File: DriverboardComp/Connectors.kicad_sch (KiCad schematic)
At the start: 14 parts, among them J26 IR Controller, J4 Kicker, J5 NUCLEO, Q6 PMOS

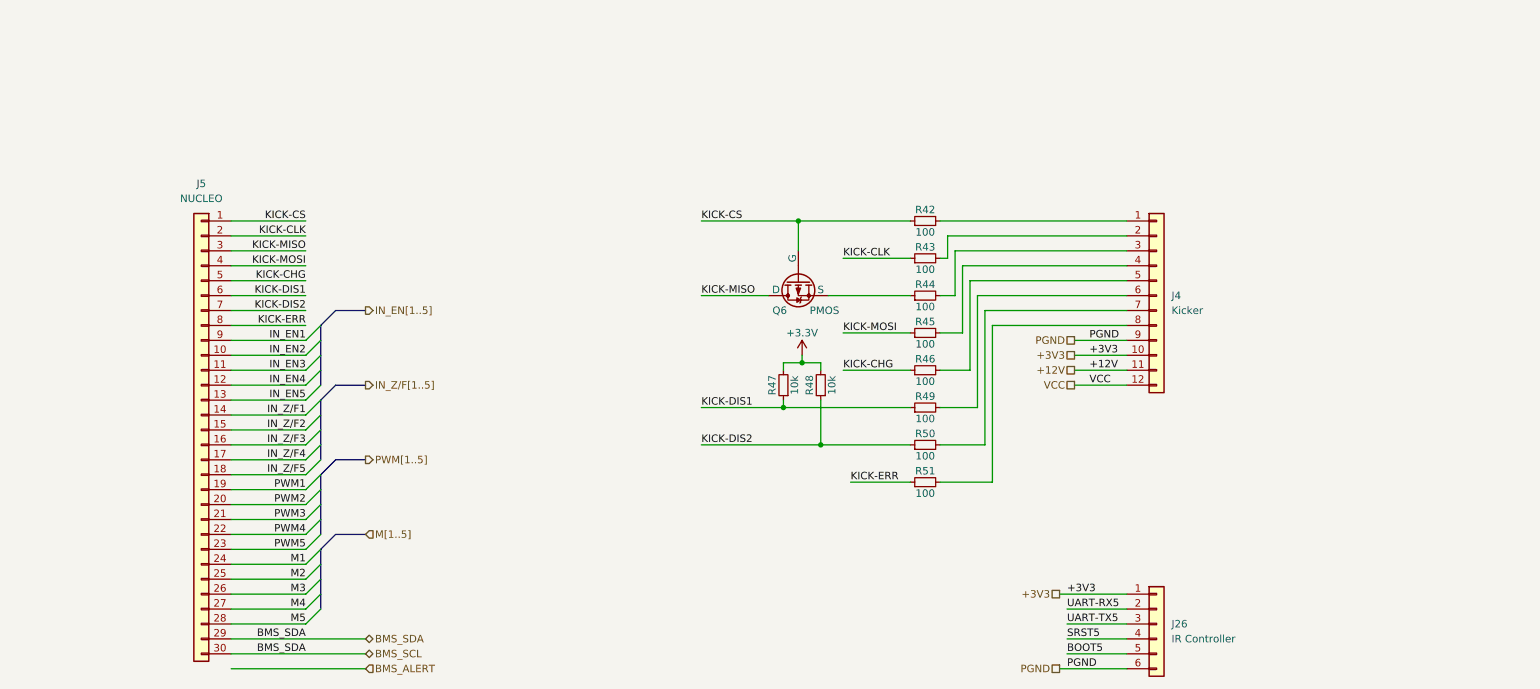
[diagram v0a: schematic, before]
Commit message: DriverboardComp is the complete design, need to be evaluated
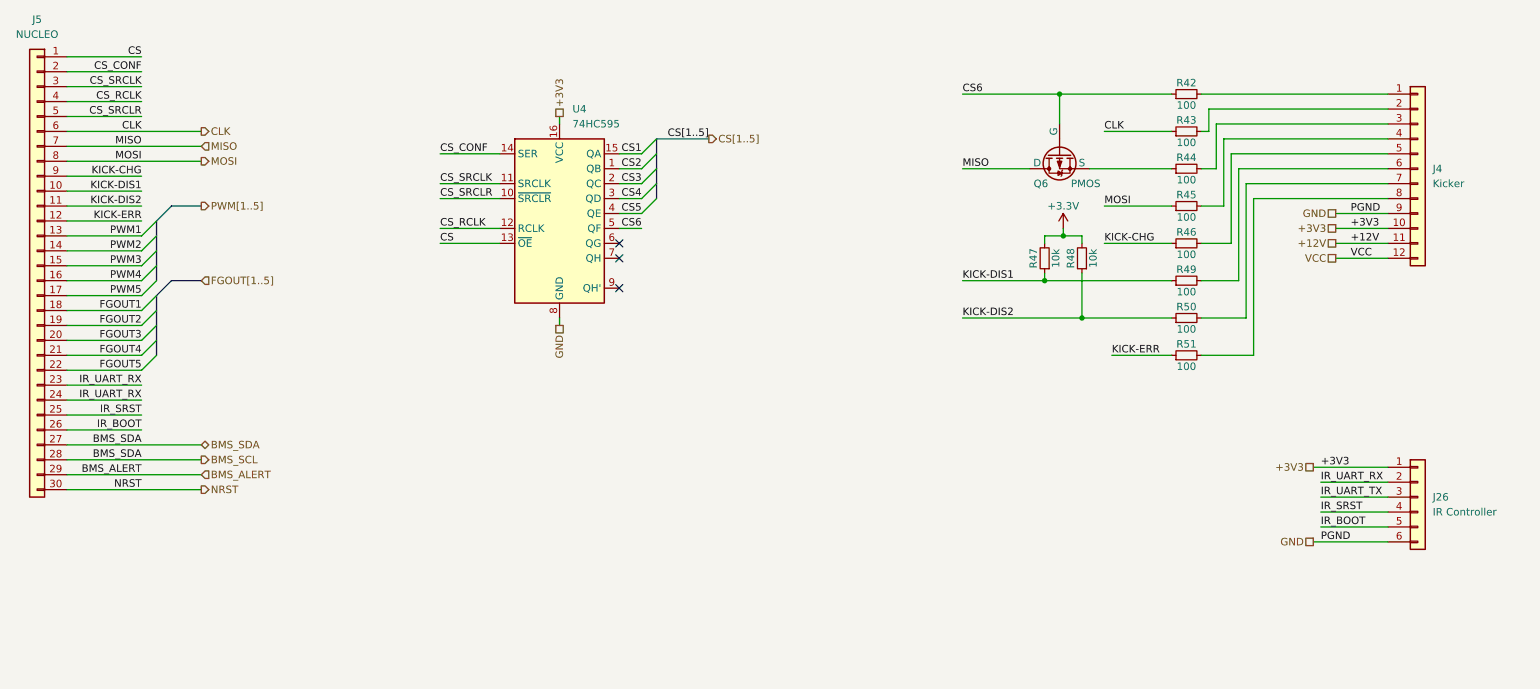
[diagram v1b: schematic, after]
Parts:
- added U4: 74HC595, symbol 74xx:74HC595
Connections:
- net IN_EN1 is gone; now on net KICK-CHG: J5.9 (Pin_9)
- net IN_EN2 is gone; now on net KICK-DIS1: J5.10 (Pin_10)
- net IN_EN3 is gone; now on net KICK-DIS2: J5.11 (Pin_11)
- net IN_EN4 is gone; now on net KICK-ERR: J5.12 (Pin_12)
- net IN_EN5 is gone; now on net PWM1: J5.13 (Pin_13)
- net IN_Z/F1 is gone; now on net PWM2: J5.14 (Pin_14)
- net IN_Z/F2 is gone; now on net PWM3: J5.15 (Pin_15)
- net IN_Z/F3 is gone; now on net PWM4: J5.16 (Pin_16)
- net IN_Z/F4 is gone; now on net PWM5: J5.17 (Pin_17)
- net M3 is gone; now on net IR_BOOT: J5.26 (Pin_26)
- net M4 is gone; now on net BMS_SCL: J5.27 (Pin_27)
- net M5 is gone; now on net BMS_SCL: J5.28 (Pin_28)
- net SRST5 is gone; now on net IR_SRST: J26.4 (Pin_4)
- net UART-RX5 is gone; now on net IR_UART_RX: J26.2 (Pin_2)
- net +3V3: now also U4.16 (VCC)
- net BMS_ALERT: now also J5.29 (Pin_29)
- net BMS_SCL: no longer J5.29 (Pin_29), J5.30 (Pin_30)
- net KICK-CHG: no longer J5.5 (Pin_5)
- net KICK-DIS1: no longer J5.6 (Pin_6)
- net KICK-DIS2: no longer J5.7 (Pin_7)
- net KICK-ERR: no longer J5.8 (Pin_8)
- net PWM1: no longer J5.19 (Pin_19)
- net PWM2: no longer J5.20 (Pin_20)
- net PWM3: no longer J5.21 (Pin_21)
- net PWM4: no longer J5.22 (Pin_22)
- net PWM5: no longer J5.23 (Pin_23)
- net BOOT5 renamed IR_BOOT
- net IN_Z/F5 renamed FGOUT1
- net KICK-CLK renamed CLK
- net CLK: now also J5.6 (Pin_6); no longer J5.2 (Pin_2)
- net KICK-CS renamed CS6
- net CS6: now also U4.5 (QF); no longer J5.1 (Pin_1)
- net KICK-MISO renamed CS_SRCLK
- net CS_SRCLK: now also U4.11 (SRCLK); no longer Q6.1 (D)
- net KICK-MOSI renamed CS_RCLK
- net CS_RCLK: now also U4.12 (RCLK); no longer R45.1
- net M1 renamed IR_UART_RX
- net IR_UART_RX: now also J5.23 (Pin_23)
- net M2 renamed IR_SRST
- net PGND renamed GND
- net GND: now also U4.8 (GND)
- net UART-TX5 renamed IR_UART_TX
- new net CS: J5.1 (Pin_1), U4.13 (~{OE})
- new net CS1: U4.15 (QA)
- new net CS2: U4.1 (QB)
- new net CS3: U4.2 (QC)
- new net CS4: U4.3 (QD)
- new net CS5: U4.4 (QE)
- new net CS_CONF: J5.2 (Pin_2), U4.14 (SER)
- new net CS_SRCLR: J5.5 (Pin_5), U4.10 (~{SRCLR})
- new net FGOUT2: J5.19 (Pin_19)
- new net FGOUT3: J5.20 (Pin_20)
- new net FGOUT4: J5.21 (Pin_21)
- new net FGOUT5: J5.22 (Pin_22)
- new net MISO: J5.7 (Pin_7), Q6.1 (D)
- new net MOSI: J5.8 (Pin_8), R45.1
- new net NRST: J5.30 (Pin_30)
- no-connect marks 0 -> 3
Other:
- moved on the sheet: J26, J4, J5, Q6, R42, R43, R44, R45, R46, R47, R48, R49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
